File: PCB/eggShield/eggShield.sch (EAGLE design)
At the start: 28 parts, among them U1 V_REG_LDOSMD, U2 V_REG_LDOSMD

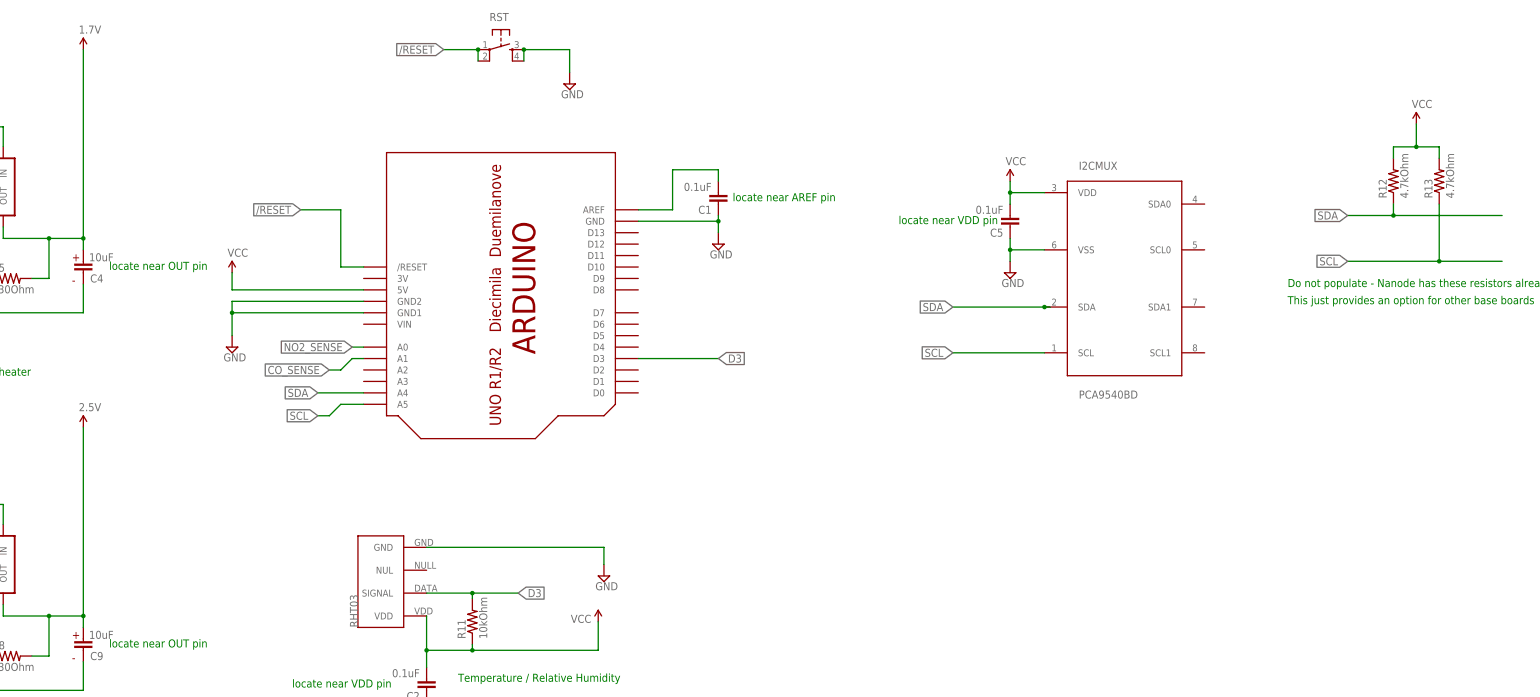
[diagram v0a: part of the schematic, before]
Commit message: rearranged some layout and routing to improve power filtering
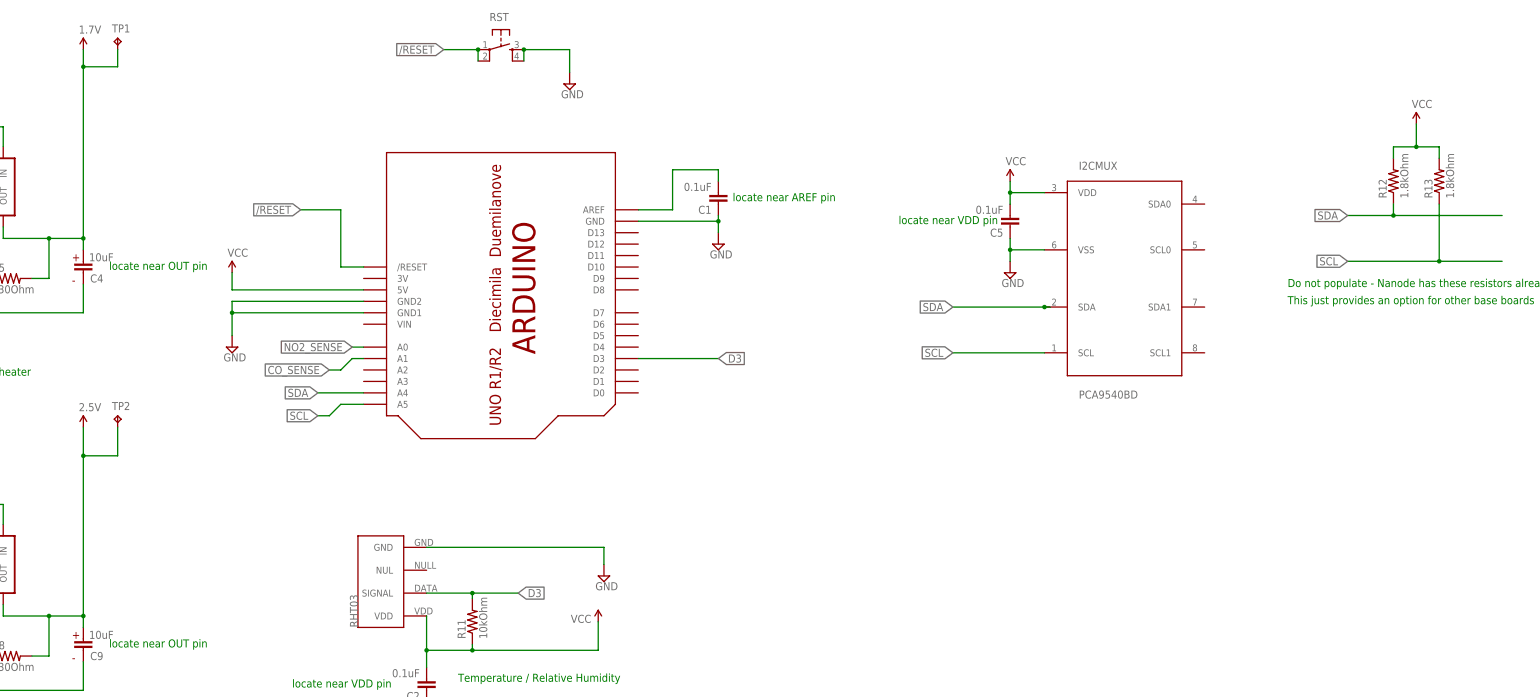
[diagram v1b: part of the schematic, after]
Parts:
- added TP1, TP2: TPPAD1-13, testpad:TPPAD1-13
- R12, R13: value 4.7kOhm -> 1.8kOhm
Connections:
- net 1.7V: now also TP1.TP
- net 2.5V: now also TP2.TP
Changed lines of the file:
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@@
 <part name="P+2" library="SparkFun" deviceset="VCC" device=""/>
 <part name="R11" library="SparkFun" deviceset="RESISTOR" device="0805-RES" value="10kOhm"/>
-<part name="R12" library="SparkFun" deviceset="RESISTOR" device="0805-RES" value="4.7kOhm"/>
-<part name="R13" library="SparkFun" deviceset="RESISTOR" device="0805-RES" value="4.7kOhm"/>
+<part name="R12" library="SparkFun" deviceset="RESISTOR" device="0805-RES" value="1.8kOhm"/>
+<part name="R13" library="SparkFun" deviceset="RESISTOR" device="0805-RES" value="1.8kOhm"/>
 <part name="P+4" library="SparkFun" deviceset="VCC" device=""/>
+<part name="TP1" library="testpad" deviceset="TP" device="PAD1-13"/>
+<part name="TP2" library="testpad" deviceset="TP" device="PAD1-13"/>
 </parts>
 <sheets>
@@
 <instance part="R13" gate="G$1" x="386.08" y="229.87" rot="R90"/>
 <instance part="P+4" gate="1" x="381" y="242.57"/>
+<instance part="TP1" gate="G$1" x="92.71" y="261.62"/>
+<instance part="TP2" gate="G$1" x="92.71" y="177.8"/>
 </instances>
 <busses>
@@
 <wire x1="77.47" y1="217.17" x2="85.09" y2="217.17" width="0.1524" layer="91"/>
 <pinref part="C4" gate="G$1" pin="1"/>
-<wire x1="85.09" y1="259.08" x2="85.09" y2="217.17" width="0.1524" layer="91"/>
+<wire x1="85.09" y1="259.08" x2="85.09" y2="255.27" width="0.1524" layer="91"/>
+<wire x1="85.09" y1="255.27" x2="85.09" y2="217.17" width="0.1524" layer="91"/>
 <wire x1="85.09" y1="214.63" x2="85.09" y2="217.17" width="0.1524" layer="91"/>
 <junction x="85.09" y="217.17"/>
@@
 <wire x1="67.31" y1="217.17" x2="77.47" y2="217.17" width="0.1524" layer="91"/>
 <junction x="77.47" y="217.17"/>
+<pinref part="TP1" gate="G$1" pin="TP"/>
+<wire x1="92.71" y1="259.08" x2="92.71" y2="255.27" width="0.1524" layer="91"/>
+<wire x1="92.71" y1="255.27" x2="85.09" y2="255.27" width="0.1524" layer="91"/>
+<junction x="85.09" y="255.27"/>
 </segment>
 <segment>
@@
 <wire x1="77.47" y1="133.35" x2="85.09" y2="133.35" width="0.1524" layer="91"/>
 <pinref part="C9" gate="G$1" pin="1"/>
-<wire x1="85.09" y1="175.26" x2="85.09" y2="133.35" width="0.1524" layer="91"/>
+<wire x1="85.09" y1="175.26" x2="85.09" y2="168.91" width="0.1524" layer="91"/>
+<wire x1="85.09" y1="168.91" x2="85.09" y2="133.35" width="0.1524" layer="91"/>
 <wire x1="85.09" y1="130.81" x2="85.09" y2="133.35" width="0.1524" layer="91"/>
 <junction x="85.09" y="133.35"/>
@@
 <wire x1="67.31" y1="133.35" x2="77.47" y2="133.35" width="0.1524" layer="91"/>
 <junction x="77.47" y="133.35"/>
-</segment>
-<segment>
+<pinref part="TP2" gate="G$1" pin="TP"/>
+<wire x1="92.71" y1="175.26" x2="92.71" y2="168.91" width="0.1524" layer="91"/>
+<wire x1="92.71" y1="168.91" x2="85.09" y2="168.91" width="0.1524" layer="91"/>
+<junction x="85.09" y="168.91"/>
+</segment>
+<segment>

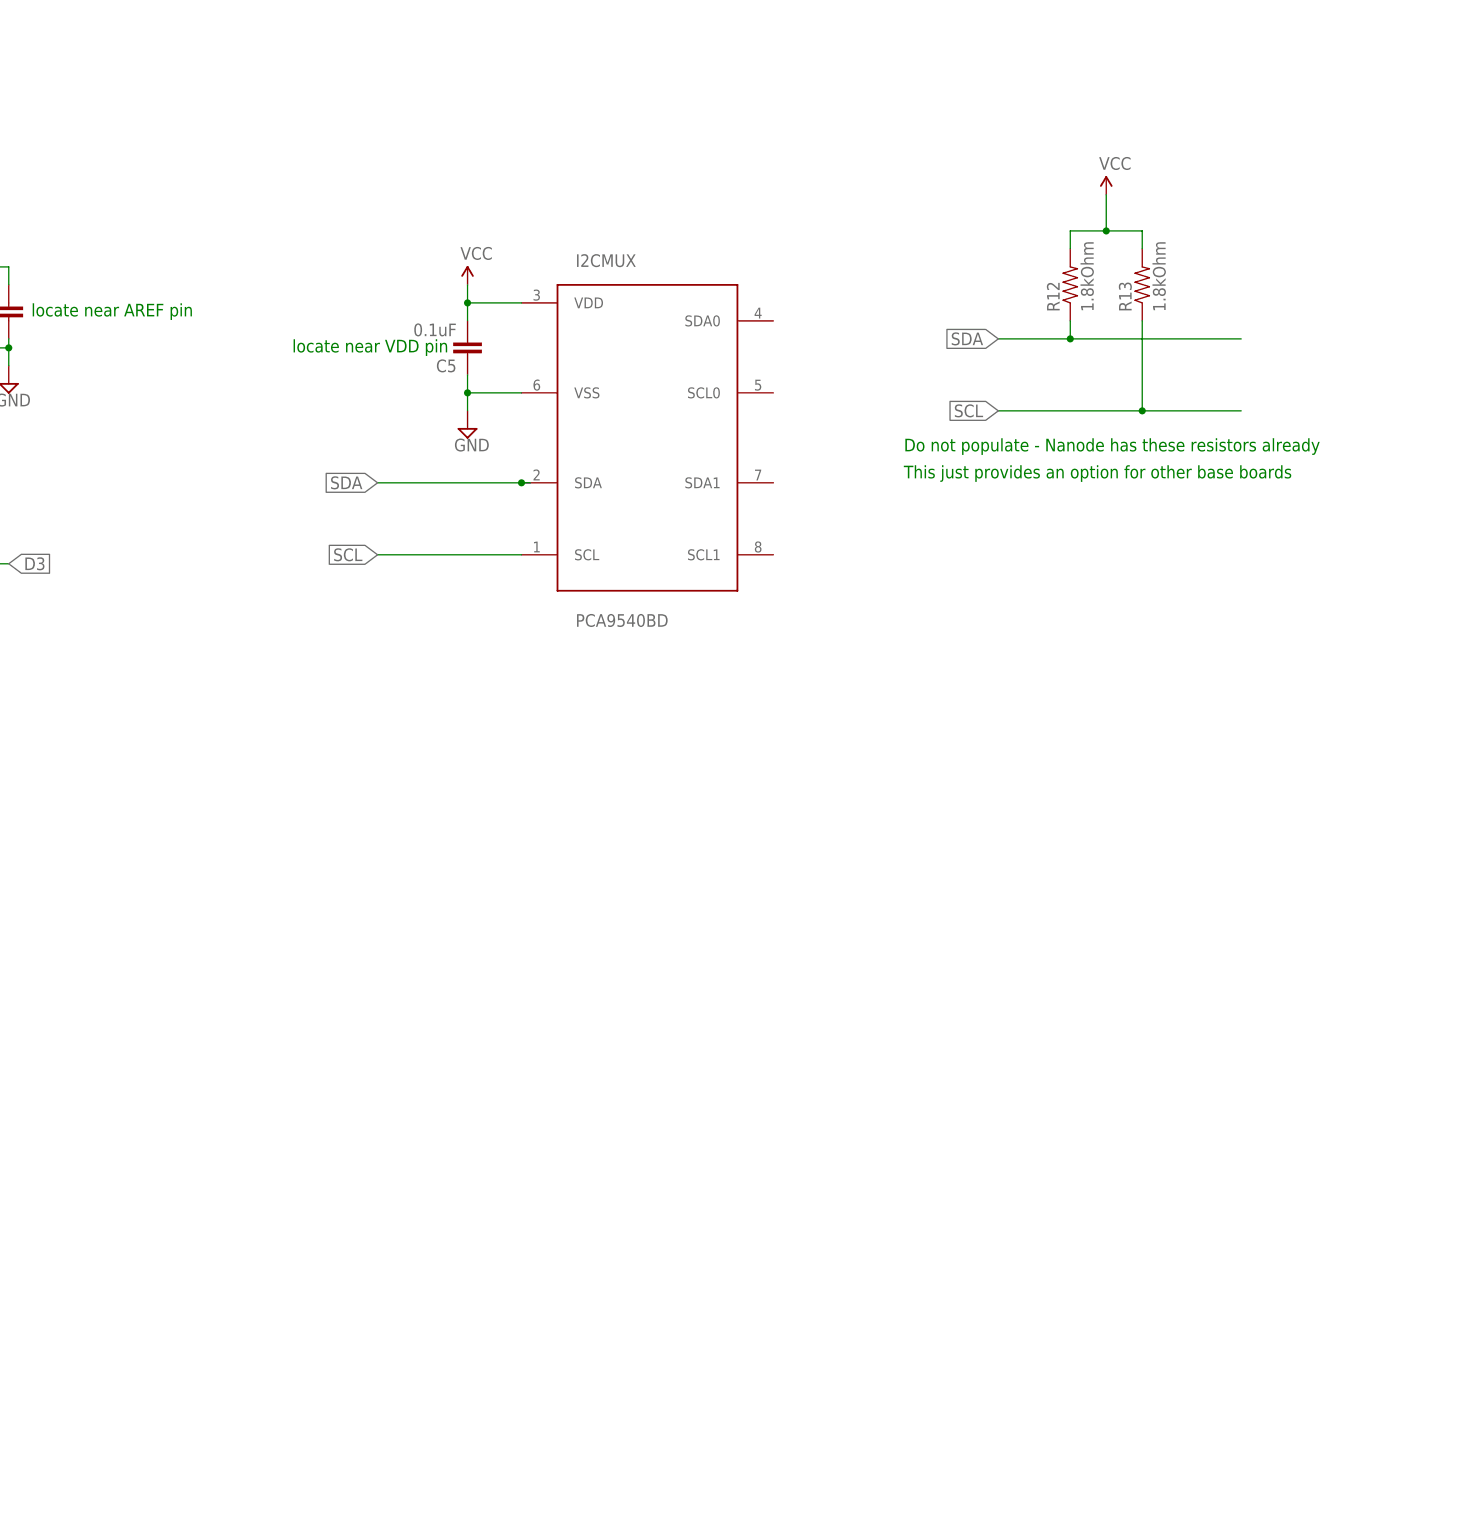
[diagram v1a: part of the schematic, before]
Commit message: added 4-pin connectors, needs to be checked against cabling; also noticed the range selection resistor taps need to be routed to arduino pins as well
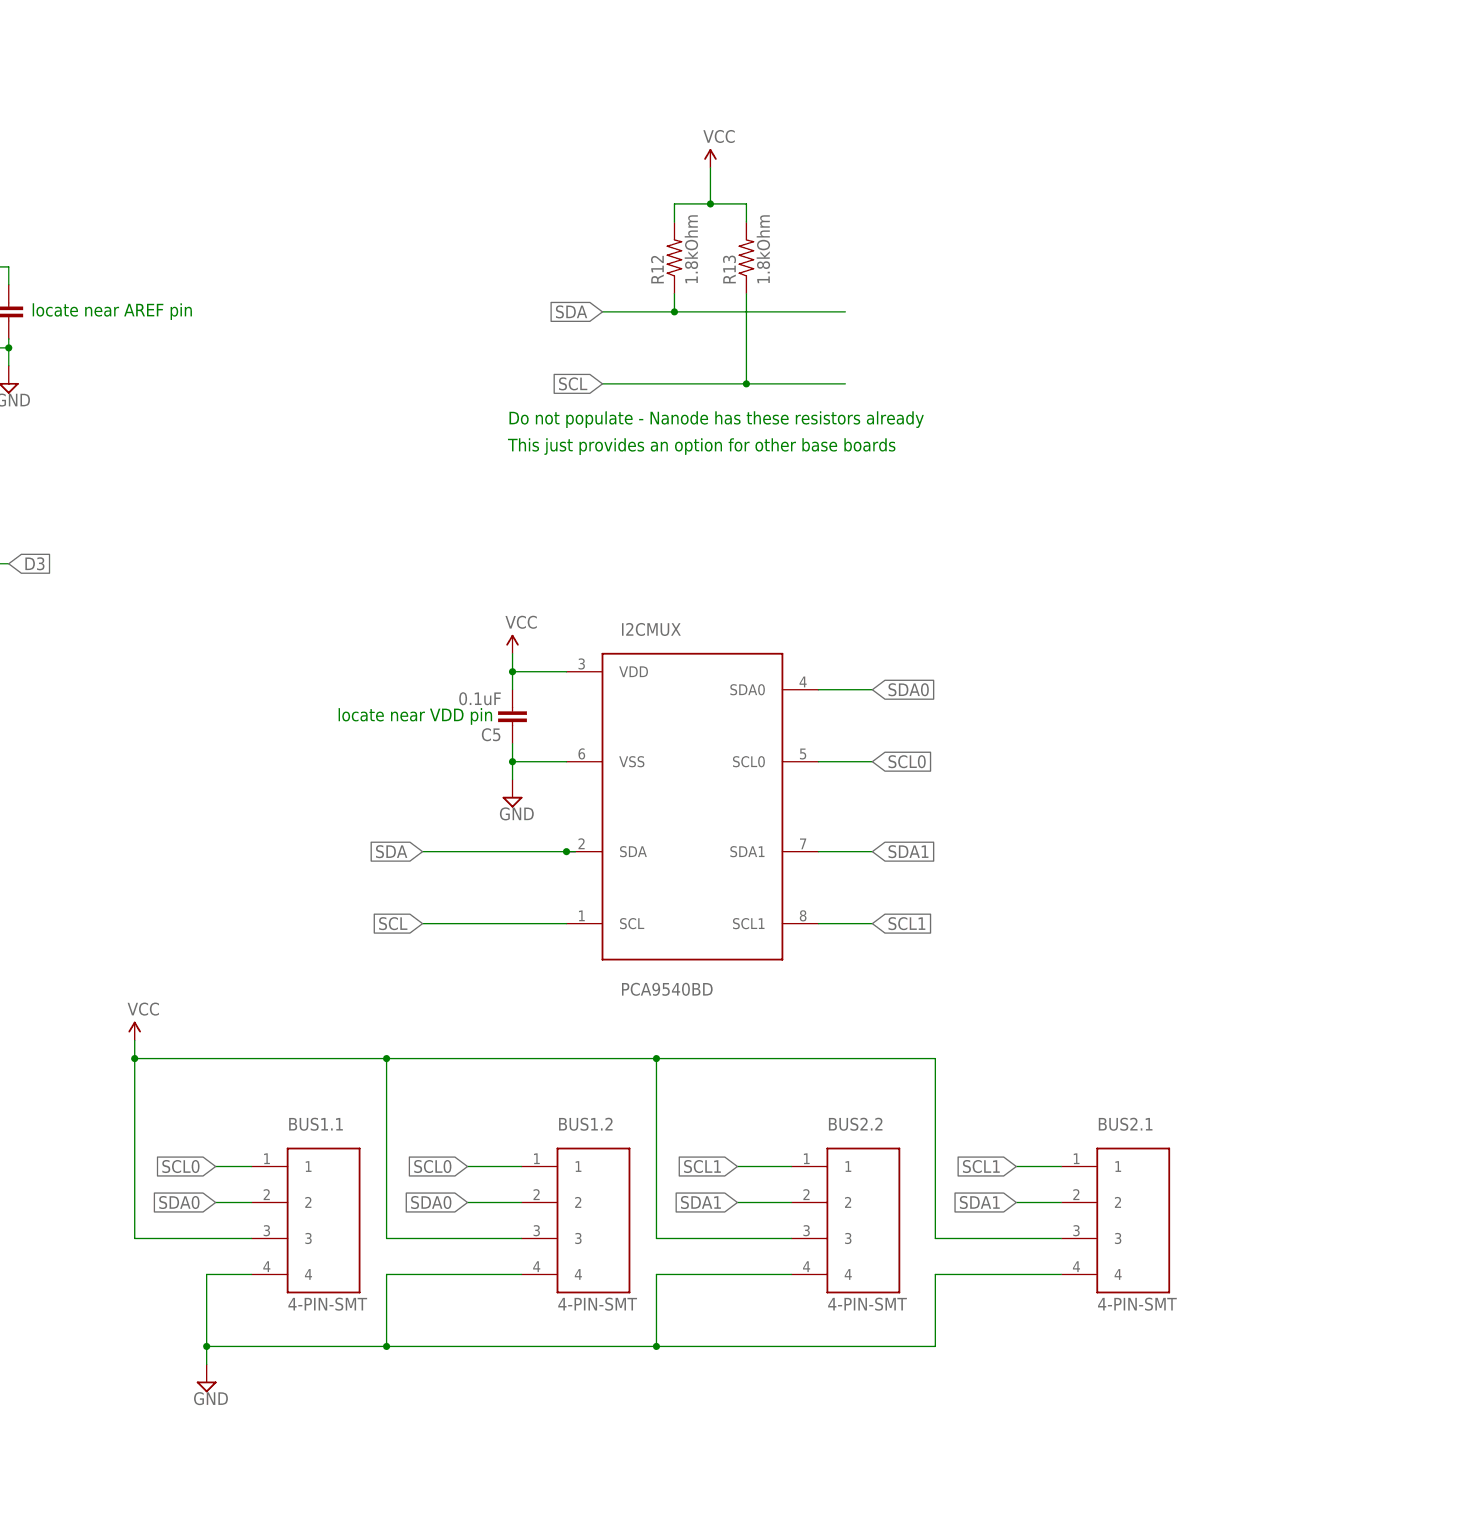
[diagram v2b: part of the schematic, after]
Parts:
- added BUS1.1, BUS1.2, BUS2.1, BUS2.2: 4-PIN-SMT, wicked-device:4-PIN-SMT
- renumbered U$2 to CO, U$4 to N02
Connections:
- new net SCL0: BUS1.1.1, BUS1.2.1, I2CMUX.SCL0
- new net SCL1: BUS2.1.1, BUS2.2.1, I2CMUX.SCL1
- new net SDA0: BUS1.1.2, BUS1.2.2, I2CMUX.SDA0
- new net SDA1: BUS2.1.2, BUS2.2.2, I2CMUX.SDA1
- net GND: now also BUS1.1.4, BUS1.2.4, BUS2.1.4, BUS2.2.4
- net VCC: now also BUS1.1.3, BUS1.2.3, BUS2.1.3, BUS2.2.3
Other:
- moved on the sheet: C5, I2CMUX, R12, R13
